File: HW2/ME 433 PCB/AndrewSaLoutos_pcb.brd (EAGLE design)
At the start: 50 x 50 mm, 23 parts

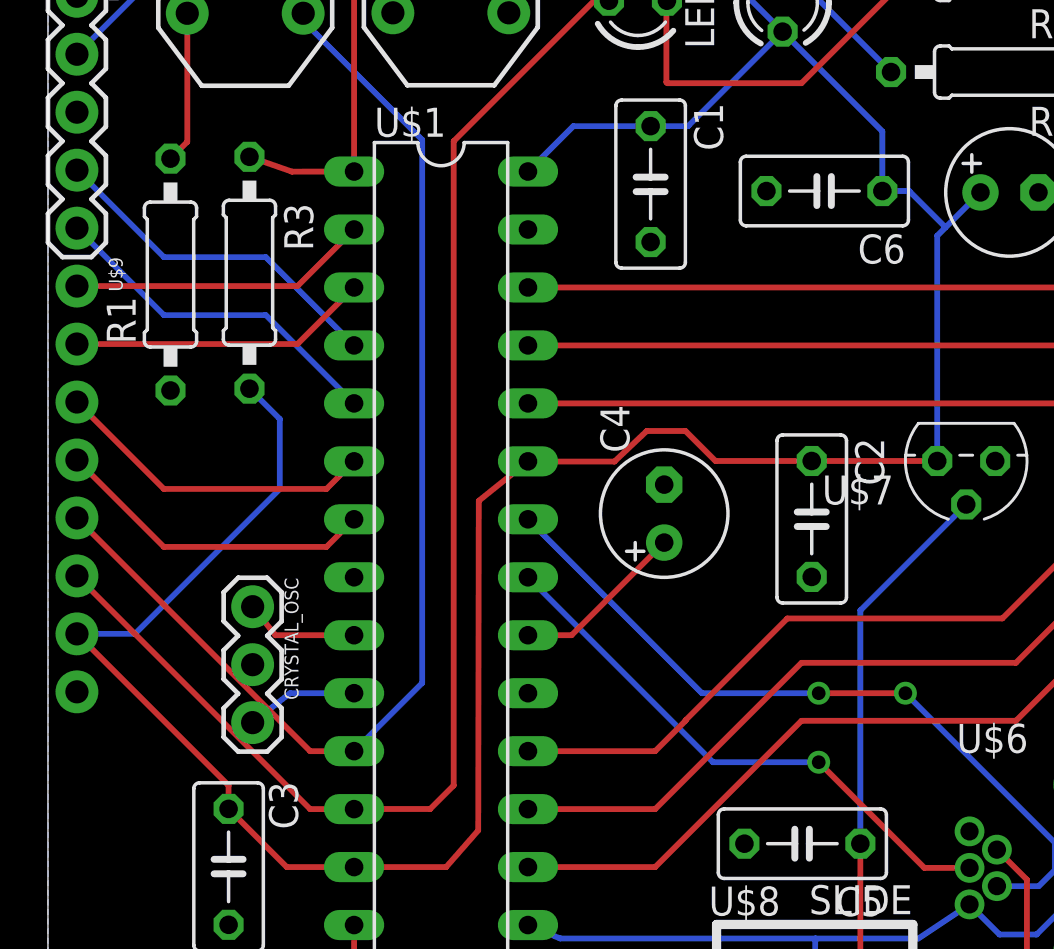
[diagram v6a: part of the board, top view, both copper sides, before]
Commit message: DRC checked with Seeed dru from master repository
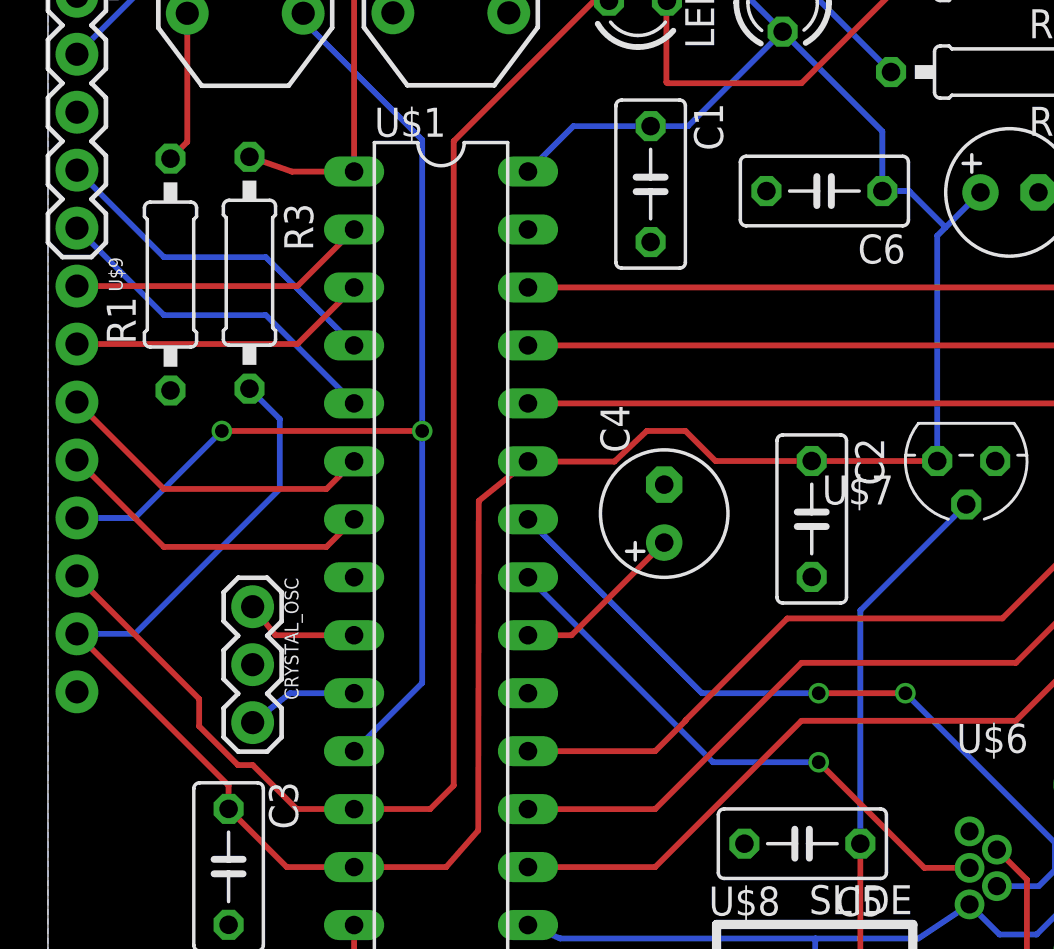
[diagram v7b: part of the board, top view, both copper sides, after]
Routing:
- net A4/LED: track 58.8 -> 59.5 mm
- net B4/USER: track 52.1 -> 52.5 mm, vias 0 -> 2
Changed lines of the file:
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@@
 </class>
 </classes>
-<designrules name="default">
+<designrules name="SeeedStudio_2layer_DRU_no_angle_20140221">
 <description language="de">&lt;b&gt;EAGLE Design Rules&lt;/b&gt;
 &lt;p&gt;
@@
 necessary adjustments and save your customized
 design rules under a new name.</description>
+<description language="zh">&lt;b&gt;Seeed Studio EAGLE Design Rules&lt;/b&gt;
+</description>
 <param name="layerSetup" value="(1*16)"/>
-<param name="mtCopper" value="0.035mm 0.035mm 0.035mm 0.035mm 0.035mm 0.035mm 0.035mm 0.035mm 0.035mm 0.035mm 0.035mm 0.035mm 0.035mm 0.035mm 0.035mm 0.035mm"/>
-<param name="mtIsolate" value="1.5mm 0.15mm 0.2mm 0.15mm 0.2mm 0.15mm 0.2mm 0.15mm 0.2mm 0.15mm 0.2mm 0.15mm 0.2mm 0.15mm 0.2mm"/>
-<param name="mdWireWire" value="8mil"/>
-<param name="mdWirePad" value="8mil"/>
-<param name="mdWireVia" value="8mil"/>
-<param name="mdPadPad" value="8mil"/>
-<param name="mdPadVia" value="8mil"/>
-<param name="mdViaVia" value="8mil"/>
-<param name="mdSmdPad" value="8mil"/>
-<param name="mdSmdVia" value="8mil"/>
-<param name="mdSmdSmd" value="8mil"/>
+<param name="mtCopper" value="0.035mm 0.0175mm 0.035mm 0.035mm 0.035mm 0.035mm 0.035mm 0.035mm 0.035mm 0.035mm 0.035mm 0.035mm 0.035mm 0.035mm 0.0175mm 0.035mm"/>
+<param name="mtIsolate" value="1.5mm 1.1mm 0.2mm 0.15mm 0.2mm 0.15mm 0.2mm 0.15mm 0.2mm 0.15mm 0.2mm 0.15mm 0.2mm 0.15mm 0.2mm"/>
+<param name="mdWireWire" value="6mil"/>
+<param name="mdWirePad" value="6mil"/>
+<param name="mdWireVia" value="6mil"/>
+<param name="mdPadPad" value="6mil"/>
+<param name="mdPadVia" value="6mil"/>
+<param name="mdViaVia" value="6mil"/>
+<param name="mdSmdPad" value="0mil"/>
+<param name="mdSmdVia" value="0mil"/>
+<param name="mdSmdSmd" value="0mil"/>
 <param name="mdViaViaSameLayer" value="8mil"/>
 <param name="mnLayersViaInSmd" value="2"/>
-<param name="mdCopperDimension" value="40mil"/>
-<param name="mdDrill" value="8mil"/>
+<param name="mdCopperDimension" value="10mil"/>
+<param name="mdDrill" value="10mil"/>
 <param name="mdSmdStop" value="0mil"/>
-<param name="msWidth" value="10mil"/>
-<param name="msDrill" value="24mil"/>
-<param name="msMicroVia" value="9.99mm"/>
+<param name="msWidth" value="6mil"/>
+<param name="msDrill" value="12mil"/>
+<param name="msMicroVia" value="12mil"/>
 <param name="msBlindViaRatio" value="0.5"/>
 <param name="rvPadTop" value="0.25"/>
@@
 <param name="rlMinPadBottom" value="10mil"/>
 <param name="rlMaxPadBottom" value="20mil"/>
-<param name="rlMinViaOuter" value="8mil"/>
+<param name="rlMinViaOuter" value="6mil"/>
 <param name="rlMaxViaOuter" value="20mil"/>
-<param name="rlMinViaInner" value="8mil"/>
+<param name="rlMinViaInner" value="6mil"/>
 <param name="rlMaxViaInner" value="20mil"/>
 <param name="rlMinMicroViaOuter" value="4mil"/>
@@
 <param name="psTop" value="-1"/>
 <param name="psBottom" value="-1"/>
-<param name="psFirst" value="-1"/>
+<param name="psFirst" value="0"/>
 <param name="psElongationLong" value="100"/>
 <param name="psElongationOffset" value="100"/>
 <param name="mvStopFrame" value="1"/>
 <param name="mvCreamFrame" value="0"/>
-<param name="mlMinStopFrame" value="4mil"/>
-<param name="mlMaxStopFrame" value="4mil"/>
+<param name="mlMinStopFrame" value="2mil"/>
+<param name="mlMaxStopFrame" value="2mil"/>
 <param name="mlMinCreamFrame" value="0mil"/>
 <param name="mlMaxCreamFrame" value="0mil"/>
-<param name="mlViaStopLimit" value="0mil"/>
+<param name="mlViaStopLimit" value="100mil"/>
 <param name="srRoundness" value="0"/>
 <param name="srMinRoundness" value="0mil"/>
@@
 <param name="checkAngle" value="0"/>
 <param name="checkFont" value="1"/>
-<param name="checkRestrict" value="1"/>
+<param name="checkRestrict" value="0"/>
 <param name="useDiameter" value="13"/>
 <param name="maxErrors" value="50"/>
@@
 <contactref element="U$1" pad="12"/>
 <contactref element="LED1" pad="A"/>
-<wire x1="13.415" y1="11.37" x2="11.49" y2="11.37" width="0.254" layer="1"/>
-<wire x1="11.49" y1="11.37" x2="1.27" y2="21.59" width="0.254" layer="1"/>
 <wire x1="24.585" y1="46.795" x2="23.935" y2="46.795" width="0.254" layer="1"/>
 <wire x1="23.935" y1="46.795" x2="17.78" y2="40.64" width="0.254" layer="1"/>
 <wire x1="17.78" y1="12.405" x2="16.75" y2="11.375" width="0.254" layer="1"/>
 <wire x1="16.75" y1="11.375" x2="13.42" y2="11.375" width="0.254" layer="1"/>
-<wire x1="13.42" y1="11.375" x2="13.415" y2="11.37" width="0.254" layer="1"/>
+<wire x1="13.415" y1="11.37" x2="13.42" y2="11.375" width="0.254" layer="1"/>
 <wire x1="17.78" y1="40.64" x2="17.78" y2="12.405" width="0.254" layer="1"/>
+<wire x1="1.27" y1="21.59" x2="1.27" y2="21.555" width="0.254" layer="1"/>
+<wire x1="1.27" y1="21.555" x2="6.625" y2="16.2" width="0.254" layer="1"/>
+<wire x1="6.625" y1="16.2" x2="6.625" y2="15" width="0.254" layer="1"/>
+<wire x1="6.625" y1="15" x2="8.325" y2="13.3" width="0.254" layer="1"/>
+<wire x1="8.325" y1="13.3" x2="8.975" y2="13.3" width="0.254" layer="1"/>
+<wire x1="8.975" y1="13.3" x2="10.9" y2="11.375" width="0.254" layer="1"/>
+<wire x1="10.9" y1="11.375" x2="13.41" y2="11.375" width="0.254" layer="1"/>
+<wire x1="13.41" y1="11.375" x2="13.415" y2="11.37" width="0.254" layer="1"/>
 </signal>
 <signal name="B4/USER">
@@
 <contactref element="USER" pad="3"/>
 <contactref element="U$1" pad="11"/>
-<wire x1="13.415" y1="13.91" x2="11.49" y2="13.91" width="0.254" layer="1"/>
-<wire x1="11.49" y1="13.91" x2="1.27" y2="24.13" width="0.254" layer="1"/>
 <wire x1="13.415" y1="13.91" x2="13.43" y2="13.925" width="0.254" layer="16"/>
 <wire x1="11.185" y1="46.245" x2="11.185" y2="45.915" width="0.254" layer="16"/>
 <wire x1="11.185" y1="45.915" x2="16.4" y2="40.7" width="0.254" layer="16"/>
-<wire x1="16.4" y1="40.7" x2="16.4" y2="16.895" width="0.254" layer="16"/>
+<wire x1="16.4" y1="40.7" x2="16.4" y2="27.94" width="0.254" layer="16"/>
+<wire x1="16.4" y1="27.94" x2="16.4" y2="16.895" width="0.254" layer="16"/>
 <wire x1="16.4" y1="16.895" x2="13.415" y2="13.91" width="0.254" layer="16"/>
+<wire x1="1.27" y1="24.13" x2="3.81" y2="24.13" width="0.254" layer="16"/>
+<wire x1="3.81" y1="24.13" x2="7.62" y2="27.94" width="0.254" layer="16"/>
+<via x="7.62" y="27.94" extent="1-16" drill="0.6"/>
+<wire x1="7.62" y1="27.94" x2="16.4" y2="27.94" width="0.254" layer="1"/>
+<via x="16.4" y="27.94" extent="1-16" drill="0.6"/>
 </signal>
 <signal name="B3">
@@
 </signal>
 </signals>
+<errors>
+</errors>
 </board>
 </drawing>
